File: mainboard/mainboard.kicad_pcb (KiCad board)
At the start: 2 copper layers, 100 x 110 mm, 428 parts, among them J1 USB_B_Micro, J2 Conn_01x02_MountingPin, J3 Conn_01x19_MountingPin, J4 Conn_01x19_MountingPin, Q1 DMG2301L, Q2 MMBT3904, Q3 MMBT3904, SW1 SW_Push, SW2 SW_Push, U1 tps63070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

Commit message: Add allignment holes
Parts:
- added REF**: Allignment_Hole, mainboard:Allignment_Hole, F.Cu at (118.5, 128.5)
- added REF**: Allignment_Hole, mainboard:Allignment_Hole, F.Cu at (21.5, 128.5)
- added REF**: Allignment_Hole, mainboard:Allignment_Hole, F.Cu at (21.5, 21.5)
- added REF**: Allignment_Hole, mainboard:Allignment_Hole, F.Cu at (118.5, 21.5)
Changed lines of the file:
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@@
     (tracks 4952)
     (zones 0)
-    (modules 428)
+    (modules 432)
     (nets 95)
   )
@@
   )
   (setup
-    (last_trace_width 0.25)
+    (last_trace_width 0.127)
     (user_trace_width 0.127)
     (user_trace_width 0.25)
@@
     (add_net VUSB)
   )
+  (module mainboard:Allignment_Hole (layer F.Cu)
+    (at 118.5 128.5)
+    (fp_text reference REF** (at 0 3.25) (layer F.SilkS) hide
+      (effects (font (size 1 1) (thickness 0.15)))
+    )
+    (fp_text value Allignment_Hole (at 0 -3.25) (layer F.Fab)
+      (effects (font (size 1 1) (thickness 0.15)))
+    )
+    (fp_circle (center 0 0) (end 2.2 0) (layer Cmts.User) (width 0.15))
+    (fp_circle (center 0 0) (end 2.45 0) (layer F.CrtYd) (width 0.05))
+    (pad "" np_thru_hole circle (at 0 0) (size 2.2 2.2) (drill 2.2) (layers *.Cu *.Paste *.Mask))
+  )
+  (module mainboard:Allignment_Hole (layer F.Cu)
+    (at 21.5 128.5)
+    (fp_text reference REF** (at 0 3.25) (layer F.SilkS) hide
+      (effects (font (size 1 1) (thickness 0.15)))
+    )
+    (fp_text value Allignment_Hole (at 0 -3.25) (layer F.Fab)
+      (effects (font (size 1 1) (thickness 0.15)))
+    )
+    (fp_circle (center 0 0) (end 2.2 0) (layer Cmts.User) (width 0.15))
+    (fp_circle (center 0 0) (end 2.45 0) (layer F.CrtYd) (width 0.05))
+    (pad "" np_thru_hole circle (at 0 0) (size 2.2 2.2) (drill 2.2) (layers *.Cu *.Paste *.Mask))
+  )
+  (module mainboard:Allignment_Hole (layer F.Cu)
+    (at 21.5 21.5)
+    (fp_text reference REF** (at 0 3.25) (layer F.SilkS) hide
+      (effects (font (size 1 1) (thickness 0.15)))
+    )
+    (fp_text value Allignment_Hole (at 0 -3.25) (layer F.Fab)
+      (effects (font (size 1 1) (thickness 0.15)))
+    )
+    (fp_circle (center 0 0) (end 2.2 0) (layer Cmts.User) (width 0.15))
+    (fp_circle (center 0 0) (end 2.45 0) (layer F.CrtYd) (width 0.05))
+    (pad "" np_thru_hole circle (at 0 0) (size 2.2 2.2) (drill 2.2) (layers *.Cu *.Paste *.Mask))
+  )
+  (module mainboard:Allignment_Hole (layer F.Cu)
+    (at 118.5 21.5)
+    (fp_text reference REF** (at 0 3.25) (layer F.SilkS) hide
+      (effects (font (size 1 1) (thickness 0.15)))
+    )
+    (fp_text value Allignment_Hole (at 0 -3.25) (layer F.Fab)
+      (effects (font (size 1 1) (thickness 0.15)))
+    )
+    (fp_circle (center 0 0) (end 2.2 0) (layer Cmts.User) (width 0.15))
+    (fp_circle (center 0 0) (end 2.45 0) (layer F.CrtYd) (width 0.05))
+    (pad "" np_thru_hole circle (at 0 0) (size 2.2 2.2) (drill 2.2) (layers *.Cu *.Paste *.Mask))
+  )
   (module Resistor_SMD:R_0805_2012Metric (layer B.Cu)

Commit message: Add revision indicator
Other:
- board text added: "Nekomimi Control-Board Panel Rev A"
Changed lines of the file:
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@@
   (general
     (thickness 1.6)
-    (drawings 292)
+    (drawings 293)
     (tracks 4952)
     (zones 0)
@@
     )
   )
+  (gr_text "Nekomimi Control-Board Panel Rev A" (at 69 128.5) (layer F.SilkS)
+    (effects (font (size 1 1) (thickness 0.15)))
+  )
   (gr_line (start 31.425 53.64) (end 33.5 53.64) (layer Edge.Cuts) (width 0.05))

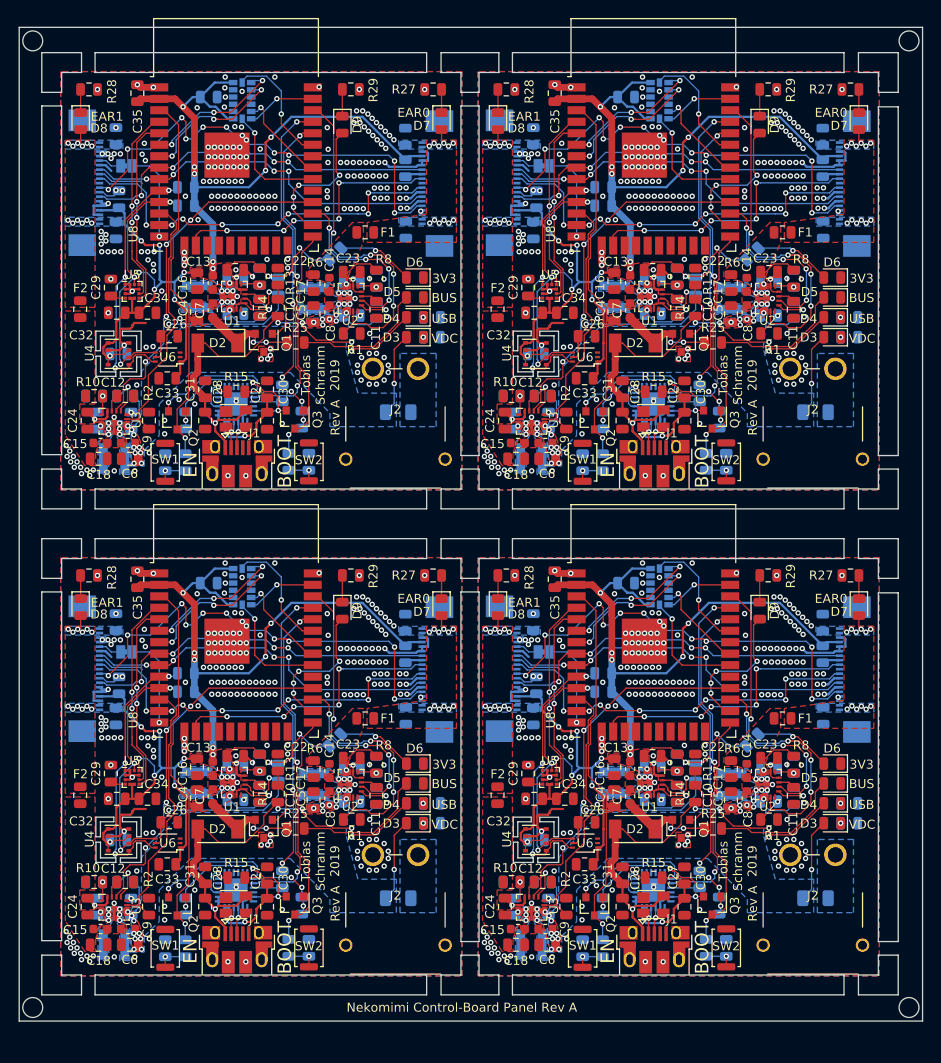
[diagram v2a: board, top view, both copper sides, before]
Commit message: Add mouse bites
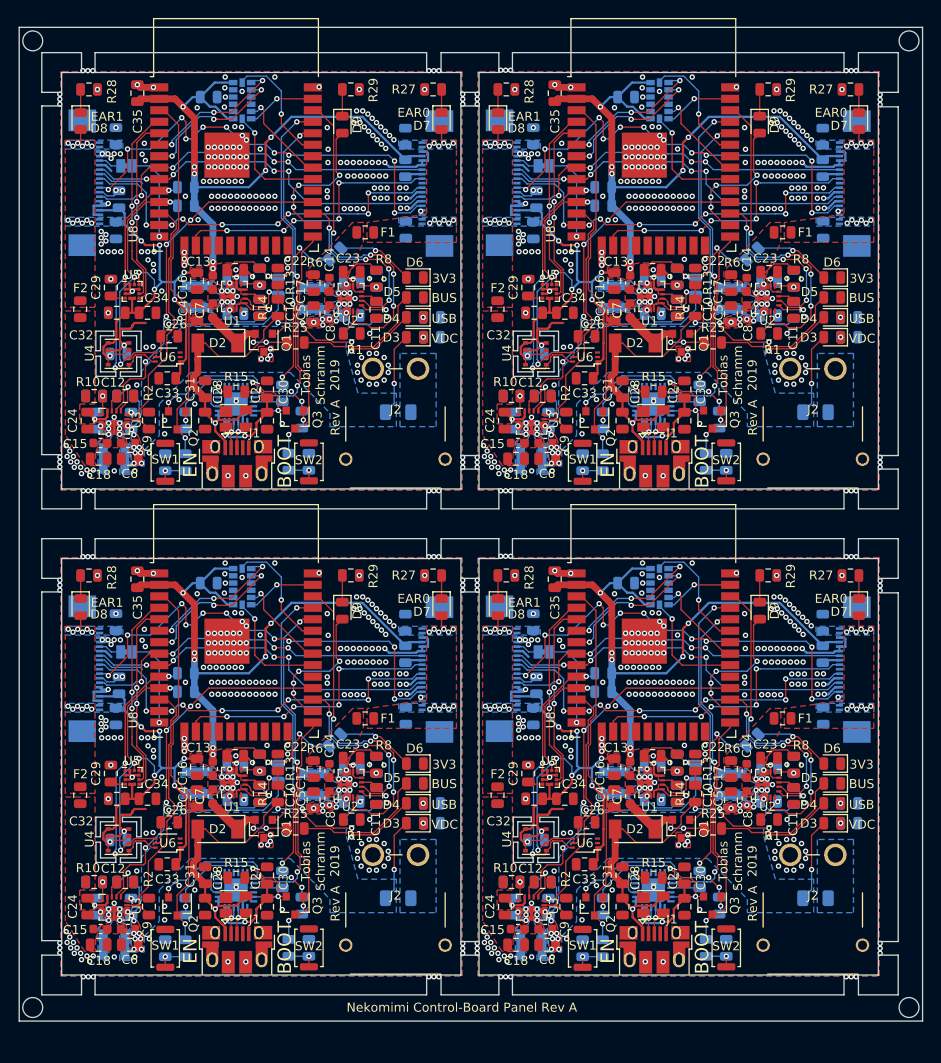
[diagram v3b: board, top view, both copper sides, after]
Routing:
- net (no net): vias 1218 -> 1314
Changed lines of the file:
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@@
     (thickness 1.6)
     (drawings 293)
-    (tracks 4952)
+    (tracks 5048)
     (zones 0)
     (modules 432)
@@
   (segment (start 49.1225 61.45) (end 49.13 61.4575) (width 0.127) (layer B.Cu) (net 0))
   (segment (start 45.9375 61.45) (end 49.1225 61.45) (width 0.127) (layer B.Cu) (net 0))
+  (via (at 69.1 81.2) (size 0.6) (drill 0.3) (layers F.Cu B.Cu) (net 0))
+  (via (at 69.1 81.75) (size 0.6) (drill 0.3) (layers F.Cu B.Cu) (net 0))
+  (via (at 69.1 82.3) (size 0.6) (drill 0.3) (layers F.Cu B.Cu) (net 0))
+  (via (at 70.7 81.2) (size 0.6) (drill 0.3) (layers F.Cu B.Cu) (net 0))
+  (via (at 70.7 82.3) (size 0.6) (drill 0.3) (layers F.Cu B.Cu) (net 0))
+  (via (at 70.7 81.75) (size 0.6) (drill 0.3) (layers F.Cu B.Cu) (net 0))
+  (via (at 70.7 121.4) (size 0.6) (drill 0.3) (layers F.Cu B.Cu) (net 0))
+  (via (at 70.7 122.5) (size 0.6) (drill 0.3) (layers F.Cu B.Cu) (net 0))
+  (via (at 70.7 121.95) (size 0.6) (drill 0.3) (layers F.Cu B.Cu) (net 0))
+  (via (at 69.1 122.5) (size 0.6) (drill 0.3) (layers F.Cu B.Cu) (net 0))
+  (via (at 69.1 121.4) (size 0.6) (drill 0.3) (layers F.Cu B.Cu) (net 0))
+  (via (at 69.1 121.95) (size 0.6) (drill 0.3) (layers F.Cu B.Cu) (net 0))
+  (via (at 24.5 81.2) (size 0.6) (drill 0.3) (layers F.Cu B.Cu) (net 0))
+  (via (at 24.5 82.3) (size 0.6) (drill 0.3) (layers F.Cu B.Cu) (net 0))
+  (via (at 24.5 81.75) (size 0.6) (drill 0.3) (layers F.Cu B.Cu) (net 0))
+  (via (at 24.5 121.35) (size 0.6) (drill 0.3) (layers F.Cu B.Cu) (net 0))
+  (via (at 24.5 122.45) (size 0.6) (drill 0.3) (layers F.Cu B.Cu) (net 0))
+  (via (at 24.5 121.9) (size 0.6) (drill 0.3) (layers F.Cu B.Cu) (net 0))
+  (via (at 27.1 125.1) (size 0.6) (drill 0.3) (layers F.Cu B.Cu) (net 0))
+  (via (at 28.2 125.1) (size 0.6) (drill 0.3) (layers F.Cu B.Cu) (net 0))
+  (via (at 27.65 125.1) (size 0.6) (drill 0.3) (layers F.Cu B.Cu) (net 0))
+  (via (at 28.15 78.6) (size 0.6) (drill 0.3) (layers F.Cu B.Cu) (net 0))
+  (via (at 27.05 78.6) (size 0.6) (drill 0.3) (layers F.Cu B.Cu) (net 0))
+  (via (at 27.6 78.6) (size 0.6) (drill 0.3) (layers F.Cu B.Cu) (net 0))
+  (via (at 66.45 78.6) (size 0.6) (drill 0.3) (layers F.Cu B.Cu) (net 0))
+  (via (at 65.35 78.6) (size 0.6) (drill 0.3) (layers F.Cu B.Cu) (net 0))
+  (via (at 65.9 78.6) (size 0.6) (drill 0.3) (layers F.Cu B.Cu) (net 0))
+  (via (at 74.4 78.55) (size 0.6) (drill 0.3) (layers F.Cu B.Cu) (net 0))
+  (via (at 73.3 78.55) (size 0.6) (drill 0.3) (layers F.Cu B.Cu) (net 0))
+  (via (at 73.85 78.55) (size 0.6) (drill 0.3) (layers F.Cu B.Cu) (net 0))
+  (via (at 112.65 78.6) (size 0.6) (drill 0.3) (layers F.Cu B.Cu) (net 0))
+  (via (at 111.55 78.6) (size 0.6) (drill 0.3) (layers F.Cu B.Cu) (net 0))
+  (via (at 112.1 78.6) (size 0.6) (drill 0.3) (layers F.Cu B.Cu) (net 0))
+  (via (at 115.3 82.35) (size 0.6) (drill 0.3) (layers F.Cu B.Cu) (net 0))
+  (via (at 115.3 81.25) (size 0.6) (drill 0.3) (layers F.Cu B.Cu) (net 0))
+  (via (at 115.3 81.8) (size 0.6) (drill 0.3) (layers F.Cu B.Cu) (net 0))
+  (via (at 115.3 122.5) (size 0.6) (drill 0.3) (layers F.Cu B.Cu) (net 0))
+  (via (at 115.3 121.4) (size 0.6) (drill 0.3) (layers F.Cu B.Cu) (net 0))
+  (via (at 115.3 121.95) (size 0.6) (drill 0.3) (layers F.Cu B.Cu) (net 0))
+  (via (at 65.35 125.1) (size 0.6) (drill 0.3) (layers F.Cu B.Cu) (net 0))
+  (via (at 66.45 125.1) (size 0.6) (drill 0.3) (layers F.Cu B.Cu) (net 0))
+  (via (at 65.9 125.1) (size 0.6) (drill 0.3) (layers F.Cu B.Cu) (net 0))
+  (via (at 73.3 125.1) (size 0.6) (drill 0.3) (layers F.Cu B.Cu) (net 0))
+  (via (at 74.4 125.1) (size 0.6) (drill 0.3) (layers F.Cu B.Cu) (net 0))
+  (via (at 73.85 125.1) (size 0.6) (drill 0.3) (layers F.Cu B.Cu) (net 0))
+  (via (at 111.55 125.1) (size 0.6) (drill 0.3) (layers F.Cu B.Cu) (net 0))
+  (via (at 112.65 125.1) (size 0.6) (drill 0.3) (layers F.Cu B.Cu) (net 0))
+  (via (at 112.1 125.1) (size 0.6) (drill 0.3) (layers F.Cu B.Cu) (net 0))
+  (via (at 28.2 71.3) (size 0.6) (drill 0.3) (layers F.Cu B.Cu) (net 0))
+  (via (at 115.3 28) (size 0.6) (drill 0.3) (layers F.Cu B.Cu) (net 0))
+  (via (at 24.5 67.55) (size 0.6) (drill 0.3) (layers F.Cu B.Cu) (net 0))
+  (via (at 28.15 24.8) (size 0.6) (drill 0.3) (layers F.Cu B.Cu) (net 0))
+  (via (at 24.5 68.65) (size 0.6) (drill 0.3) (layers F.Cu B.Cu) (net 0))
+  (via (at 24.5 68.1) (size 0.6) (drill 0.3) (layers F.Cu B.Cu) (net 0))
+  (via (at 27.65 71.3) (size 0.6) (drill 0.3) (layers F.Cu B.Cu) (net 0))
+  (via (at 66.45 71.3) (size 0.6) (drill 0.3) (layers F.Cu B.Cu) (net 0))
+  (via (at 70.7 27.95) (size 0.6) (drill 0.3) (layers F.Cu B.Cu) (net 0))
+  (via (at 70.7 68.7) (size 0.6) (drill 0.3) (layers F.Cu B.Cu) (net 0))
+  (via (at 70.7 28.5) (size 0.6) (drill 0.3) (layers F.Cu B.Cu) (net 0))
+  (via (at 115.3 27.45) (size 0.6) (drill 0.3) (layers F.Cu B.Cu) (net 0))
+  (via (at 66.45 24.8) (size 0.6) (drill 0.3) (layers F.Cu B.Cu) (net 0))
+  (via (at 24.5 28.5) (size 0.6) (drill 0.3) (layers F.Cu B.Cu) (net 0))
+  (via (at 65.9 71.3) (size 0.6) (drill 0.3) (layers F.Cu B.Cu) (net 0))
+  (via (at 115.3 67.6) (size 0.6) (drill 0.3) (layers F.Cu B.Cu) (net 0))
+  (via (at 24.5 27.95) (size 0.6) (drill 0.3) (layers F.Cu B.Cu) (net 0))
+  (via (at 112.1 24.8) (size 0.6) (drill 0.3) (layers F.Cu B.Cu) (net 0))
+  (via (at 27.1 71.3) (size 0.6) (drill 0.3) (layers F.Cu B.Cu) (net 0))
+  (via (at 112.65 24.8) (size 0.6) (drill 0.3) (layers F.Cu B.Cu) (net 0))
+  (via (at 112.65 71.3) (size 0.6) (drill 0.3) (layers F.Cu B.Cu) (net 0))
+  (via (at 65.35 71.3) (size 0.6) (drill 0.3) (layers F.Cu B.Cu) (net 0))
+  (via (at 70.7 67.6) (size 0.6) (drill 0.3) (layers F.Cu B.Cu) (net 0))
+  (via (at 73.85 71.3) (size 0.6) (drill 0.3) (layers F.Cu B.Cu) (net 0))
+  (via (at 74.4 71.3) (size 0.6) (drill 0.3) (layers F.Cu B.Cu) (net 0))
+  (via (at 27.6 24.8) (size 0.6) (drill 0.3) (layers F.Cu B.Cu) (net 0))
+  (via (at 65.9 24.8) (size 0.6) (drill 0.3) (layers F.Cu B.Cu) (net 0))
+  (via (at 69.1 68.15) (size 0.6) (drill 0.3) (layers F.Cu B.Cu) (net 0))
+  (via (at 74.4 24.75) (size 0.6) (drill 0.3) (layers F.Cu B.Cu) (net 0))
+  (via (at 115.3 68.15) (size 0.6) (drill 0.3) (layers F.Cu B.Cu) (net 0))
+  (via (at 115.3 68.7) (size 0.6) (drill 0.3) (layers F.Cu B.Cu) (net 0))
+  (via (at 73.85 24.75) (size 0.6) (drill 0.3) (layers F.Cu B.Cu) (net 0))
+  (via (at 112.1 71.3) (size 0.6) (drill 0.3) (layers F.Cu B.Cu) (net 0))
+  (via (at 65.35 24.8) (size 0.6) (drill 0.3) (layers F.Cu B.Cu) (net 0))
+  (via (at 27.05 24.8) (size 0.6) (drill 0.3) (layers F.Cu B.Cu) (net 0))
+  (via (at 73.3 24.75) (size 0.6) (drill 0.3) (layers F.Cu B.Cu) (net 0))
+  (via (at 24.5 27.4) (size 0.6) (drill 0.3) (layers F.Cu B.Cu) (net 0))
+  (via (at 115.3 28.55) (size 0.6) (drill 0.3) (layers F.Cu B.Cu) (net 0))
+  (via (at 69.1 28.5) (size 0.6) (drill 0.3) (layers F.Cu B.Cu) (net 0))
+  (via (at 69.1 27.4) (size 0.6) (drill 0.3) (layers F.Cu B.Cu) (net 0))
+  (via (at 69.1 27.95) (size 0.6) (drill 0.3) (layers F.Cu B.Cu) (net 0))
+  (via (at 69.1 68.7) (size 0.6) (drill 0.3) (layers F.Cu B.Cu) (net 0))
+  (via (at 69.1 67.6) (size 0.6) (drill 0.3) (layers F.Cu B.Cu) (net 0))
+  (via (at 70.7 68.15) (size 0.6) (drill 0.3) (layers F.Cu B.Cu) (net 0))
+  (via (at 111.55 71.3) (size 0.6) (drill 0.3) (layers F.Cu B.Cu) (net 0))
+  (via (at 73.3 71.3) (size 0.6) (drill 0.3) (layers F.Cu B.Cu) (net 0))
+  (via (at 70.7 27.4) (size 0.6) (drill 0.3) (layers F.Cu B.Cu) (net 0))
+  (via (at 111.55 24.8) (size 0.6) (drill 0.3) (layers F.Cu B.Cu) (net 0))
   (via (at 64.45 94.15) (size 0.6) (drill 0.3) (layers F.Cu B.Cu) (net 1))
   (via (at 53.2 80.4) (size 0.6) (drill 0.3) (layers F.Cu B.Cu) (net 1))

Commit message: Trim PCB to 100 x 100 mm
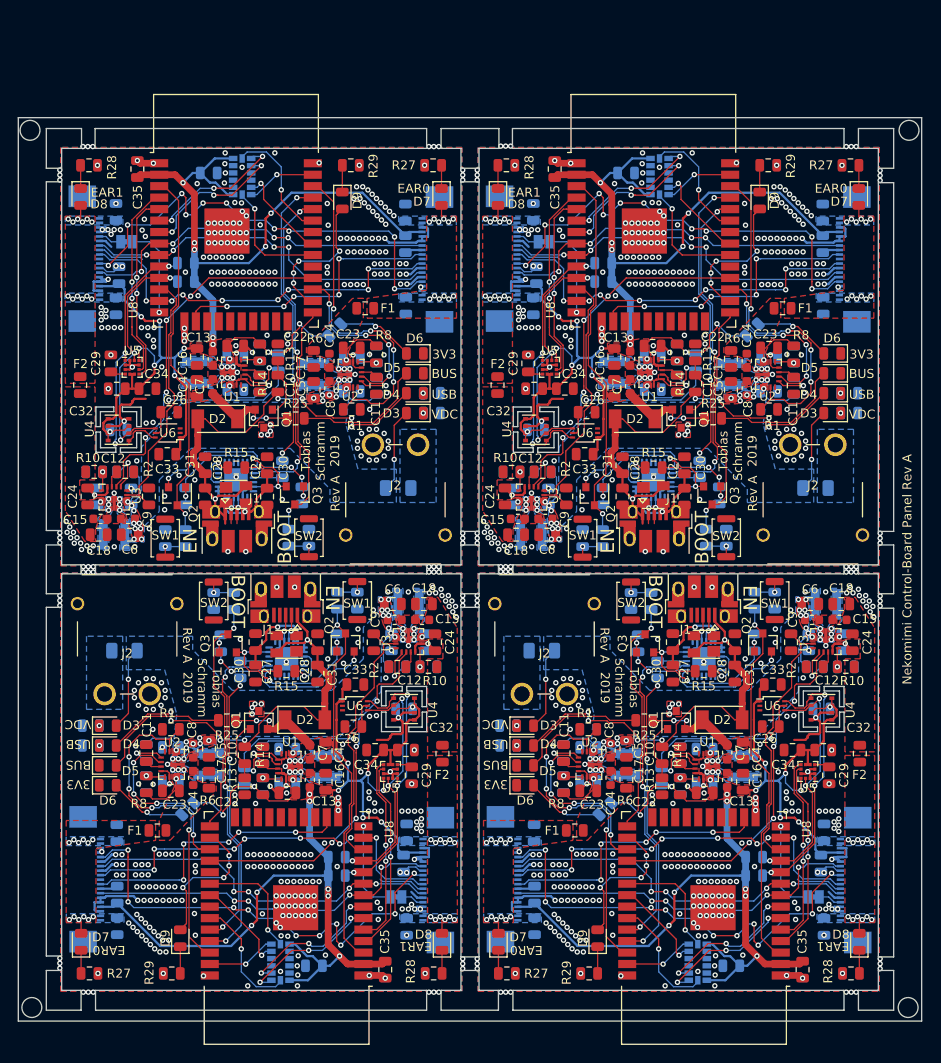
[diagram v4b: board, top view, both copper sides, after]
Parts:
- moved R28 95.2 mm to (112.1, 124.7), turned to 180 degrees
- moved R27 95.1 mm to (27.8, 124.7), turned to 0 degrees
- moved D8 93.8 mm to (113.0, 121.2), turned to 90 degrees
- moved D7 93.7 mm to (26.9, 121.2), turned to 90 degrees
- moved C18 90.4 mm to (111.0, 83.8), turned to 180 degrees
- moved C24 89.6 mm to (112.2, 88.1), turned to 270 degrees
- moved C15 88.7 mm to (110.8, 85.6), turned to 180 degrees
- moved C21 87.6 mm to (111.2, 88.1), turned to 270 degrees
- moved L3 87.3 mm to (109.3, 83.9), turned to 0 degrees
- moved R10 86.5 mm to (111.5, 90.8), turned to 0 degrees
- moved R11 86.5 mm to (111.5, 90.8), turned to 0 degrees
- moved F2 86.4 mm to (113.0, 100.4), turned to 90 degrees
- moved C35 85.4 mm to (106.7, 124.3), turned to 270 degrees
- moved C43 85.3 mm to (109.1, 119.6), turned to 270 degrees
- moved J4 85.2 mm to (110.9, 114.3), turned to 270 degrees
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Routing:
- net (no net): vias 1314 -> 1312
- net GND: vias 216 -> 218
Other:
- board size 100 x 110 mm -> 100 x 100 mm
